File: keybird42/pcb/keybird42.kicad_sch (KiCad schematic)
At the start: 177 parts, among them SW111 SW_MX, SW112 SW_MX, SW113 SW_MX, SW114 SW_MX, SW115 SW_MX, SW116 SW_MX, SW117 SW_MX, SW121 SW_MX, SW122 SW_MX, SW123 SW_MX, SW124 SW_MX, SW125 SW_MX, SW126 SW_MX, SW127 SW_MX, SW131 SW_MX, SW132 SW_MX, SW133 SW_MX, SW134 SW_MX, SW135 SW_MX, SW136 SW_MX, SW137 SW_MX, SW211 SW_MX, SW212 SW_MX, SW213 SW_MX, SW214 SW_MX, SW215 SW_MX, SW216 SW_MX, SW217 SW_MX, SW221 SW_MX, SW222 SW_MX, SW223 SW_MX, SW225 SW_MX, SW226 SW_MX, SW227 SW_MX, SW231 SW_MX, SW232 SW_MX, SW233 SW_MX, SW234 SW_MX, SW235 SW_MX, SW236 SW_MX, SW237 SW_MX, SW311 SW_MX, SW312 SW_MX, SW314 SW_MX, SW315 SW_MX, SW316 SW_MX, SW317 SW_MX, SW321 SW_MX, SW322 SW_MX, SW323 SW_MX, SW324 SW_MX, SW325 SW_MX, SW327 SW_MX, SW331 SW_MX, SW332 SW_MX, SW333 SW_MX, SW334 SW_MX, SW335 SW_MX, SW336 SW_MX, SW337 SW_MX, SW411 SW_MX, SW412 SW_MX, SW413 SW_MX, SW414 SW_MX, SW415 SW_MX, SW416 SW_MX, SW417 SW_MX, SW421 SW_MX, SW422 SW_MX, SW423 SW_MX, SW424 SW_MX, SW425 SW_MX, SW426 SW_MX, SW427 SW_MX, SW431 SW_MX, SW432 SW_MX, SW433 SW_MX, SW434 SW_MX, SW435 SW_MX, SW436 SW_MX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

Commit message: rough positioning of row 4, two more holes
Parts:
- removed D422, D435: 1N4148W, Diode_SMD:D_SOD-123, symbol keybird42:1N4148W
- removed SW422, SW435: SW_MX, PCM_Switch_Keyboard_Hotswap_Kailh:SW_Hotswap_Kailh_MX, symbol keybird42:SW_MX
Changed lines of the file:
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@@
   (junction (at 113.03 177.8) (diameter 0) (color 0 0 0 0)
   )
-  (junction (at 57.15 152.4) (diameter 0) (color 0 0 0 0)
-  )
   (junction (at 74.93 157.48) (diameter 0) (color 0 0 0 0)
   )
@@
   (junction (at 57.15 76.2) (diameter 0) (color 0 0 0 0)
   )
-  (junction (at 46.99 144.78) (diameter 0) (color 0 0 0 0)
-  )
   (junction (at 43.18 177.8) (diameter 0) (color 0 0 0 0)
   )
@@
   (junction (at 113.03 63.5) (diameter 0) (color 0 0 0 0)
   )
-  (junction (at 99.06 165.1) (diameter 0) (color 0 0 0 0)
-  )
   (junction (at 74.93 55.88) (diameter 0) (color 0 0 0 0)
   )
@@
   (junction (at 60.96 55.88) (diameter 0) (color 0 0 0 0)
   )
-  (junction (at 88.9 157.48) (diameter 0) (color 0 0 0 0)
-  )
   (junction (at 71.12 127) (diameter 0) (color 0 0 0 0)
   )
@@
     (stroke (width 0) (type default))
   )
-  (wire (pts (xy 88.9 157.48) (xy 88.9 170.18))
+  (wire (pts (xy 88.9 144.78) (xy 88.9 170.18))
     (stroke (width 0) (type default))
   )
@@
     (stroke (width 0) (type default))
   )
-  (wire (pts (xy 85.09 165.1) (xy 99.06 165.1))
+  (wire (pts (xy 85.09 165.1) (xy 113.03 165.1))
     (stroke (width 0) (type default))
   )
@@
     (stroke (width 0) (type default))
   )
-  (wire (pts (xy 99.06 165.1) (xy 113.03 165.1))
-    (stroke (width 0) (type default))
-  )
-  (wire (pts (xy 46.99 144.78) (xy 46.99 157.48))
-    (stroke (width 0) (type default))
-  )
   (wire (pts (xy 57.15 177.8) (xy 71.12 177.8))
     (stroke (width 0) (type default))
@@
     (stroke (width 0) (type default))
   )
-  (wire (pts (xy 43.18 152.4) (xy 57.15 152.4))
-    (stroke (width 0) (type default))
-  )
   (wire (pts (xy 33.02 43.18) (xy 33.02 55.88))
     (stroke (width 0) (type default))
@@
     (stroke (width 0) (type default))
   )
-  (wire (pts (xy 46.99 132.08) (xy 46.99 144.78))
+  (wire (pts (xy 46.99 132.08) (xy 46.99 157.48))
     (stroke (width 0) (type default))
   )
@@
     (stroke (width 0) (type default))
   )
-  (wire (pts (xy 57.15 152.4) (xy 71.12 152.4))
+  (wire (pts (xy 43.18 152.4) (xy 71.12 152.4))
     (stroke (width 0) (type default))
   )
@@
     (stroke (width 0) (type default))
   )
-  (wire (pts (xy 88.9 144.78) (xy 88.9 157.48))
-    (stroke (width 0) (type default))
-  )
   (wire (pts (xy 85.09 114.3) (xy 99.06 114.3))
     (stroke (width 0) (type default))
@@
     )
   )
-  (symbol (lib_id "keybird42:SW_MX") (at 93.98 157.48 0) (unit 1)
-    (in_bom yes) (on_board yes) (dnp no)
-    (property "Reference" "SW435" (at 96.52 159.385 0) (do_not_autoplace)
-      (effects (font (size 1.27 1.27)) (justify right))
-    )
-    (property "Value" "SW_MX" (at 93.98 152.4 0)
-      (effects (font (size 1.27 1.27)) hide)
-    )
-    (property "Footprint" "PCM_Switch_Keyboard_Hotswap_Kailh:SW_Hotswap_Kailh_MX" (at 93.98 149.86 0)
-      (effects (font (size 1.27 1.27)) hide)
-    )
-    (property "Datasheet" "~" (at 93.98 152.4 0)
-      (effects (font (size 1.27 1.27)) hide)
-    )
-    (pin "2")
-    (pin "1")
-    (instances
-      (project "keybird42"
-        (path "/c6489b6f-cd36-4929-9d41-a438ed9c3e88"
-          (reference "SW435") (unit 1)
-        )
-      )
-    )
-  )
   (symbol (lib_id "keybird42:SW_MX") (at 93.98 17.78 0) (unit 1)
     (in_bom yes) (on_board yes) (dnp no)
@@
     )
   )
-  (symbol (lib_id "keybird42:SW_MX") (at 52.07 144.78 0) (unit 1)
-    (in_bom yes) (on_board yes) (dnp no)
-    (property "Reference" "SW422" (at 54.61 146.685 0) (do_not_autoplace)
-      (effects (font (size 1.27 1.27)) (justify right))
-    )
-    (property "Value" "SW_MX" (at 52.07 139.7 0)
-      (effects (font (size 1.27 1.27)) hide)
-    )
-    (property "Footprint" "PCM_Switch_Keyboard_Hotswap_Kailh:SW_Hotswap_Kailh_MX" (at 52.07 137.16 0)
-      (effects (font (size 1.27 1.27)) hide)
-    )
-    (property "Datasheet" "~" (at 52.07 139.7 0)
-      (effects (font (size 1.27 1.27)) hide)
-    )
-    (pin "2")
-    (pin "1")
-    (instances
-      (project "keybird42"
-        (path "/c6489b6f-cd36-4929-9d41-a438ed9c3e88"
-          (reference "SW422") (unit 1)
-        )
-      )
-    )
-  )
   (symbol (lib_id "keybird42:1N4148W") (at 57.15 59.69 0) (unit 1)
     (in_bom yes) (on_board yes) (dnp no) (fields_autoplaced)
@@
     )
   )
-  (symbol (lib_id "keybird42:1N4148W") (at 99.06 161.29 0) (unit 1)
-    (in_bom yes) (on_board yes) (dnp no) (fields_autoplaced)
-    (property "Reference" "D435" (at 96.52 162.56 0) (do_not_autoplace)
-      (effects (font (size 1.27 1.27)) (justify right))
-    )
-    (property "Value" "1N4148W" (at 99.06 168.91 0)
-      (effects (font (size 1.27 1.27)) hide)
-    )
-    (property "Footprint" "Diode_SMD:D_SOD-123" (at 99.06 171.45 0)
-      (effects (font (size 1.27 1.27)) hide)
-    )
-    (property "Datasheet" "https://www.vishay.com/docs/85748/1n4148w.pdf" (at 99.06 173.99 0)
-      (effects (font (size 1.27 1.27)) hide)
-    )
-    (property "Sim.Device" "D" (at 99.06 166.37 0)
-      (effects (font (size 1.27 1.27)) hide)
-    )
-    (property "Sim.Pins" "1=K 2=A" (at 102.87 161.29 90)
-      (effects (font (size 1.27 1.27)) hide)
-    )
-    (pin "1")
-    (pin "2")
-    (instances
-      (project "keybird42"
-        (path "/c6489b6f-cd36-4929-9d41-a438ed9c3e88"
-          (reference "D435") (unit 1)
-        )
-      )
-    )
-  )
   (symbol (lib_id "keybird42:1N4148W") (at 71.12 110.49 0) (unit 1)
     (in_bom yes) (on_board yes) (dnp no) (fields_autoplaced)
@@
         )
       )
-    )
-  )
-  (symbol (lib_id "keybird42:1N4148W") (at 57.15 148.59 0) (unit 1)
-    (in_bom yes) (on_board yes) (dnp no) (fields_autoplaced)
-    (property "Reference" "D422" (at 54.61 149.86 0) (do_not_autoplace)
-      (effects (font (size 1.27 1.27)) (justify right))
-    )
-    (property "Value" "1N4148W" (at 57.15 156.21 0)
-      (effects (font (size 1.27 1.27)) hide)
-    )
-    (property "Footprint" "Diode_SMD:D_SOD-123" (at 57.15 158.75 0)
-      (effects (font (size 1.27 1.27)) hide)
-    )
-    (property "Datasheet" "https://www.vishay.com/docs/85748/1n4148w.pdf" (at 57.15 161.29 0)
-      (effects (font (size 1.27 1.27)) hide)
-    )
-    (property "Sim.Device" "D" (at 57.15 153.67 0)
-      (effects (font (size 1.27 1.27)) hide)
-    )
-    (property "Sim.Pins" "1=K 2=A" (at 60.96 148.59 90)
-      (effects (font (size 1.27 1.27)) hide)
-    )
-    (pin "1")
-    (pin "2")
-    (instances
-      (project "keybird42"
-        (path "/c6489b6f-cd36-4929-9d41-a438ed9c3e88"
-          (reference "D422") (unit 1)
-        )
-      )

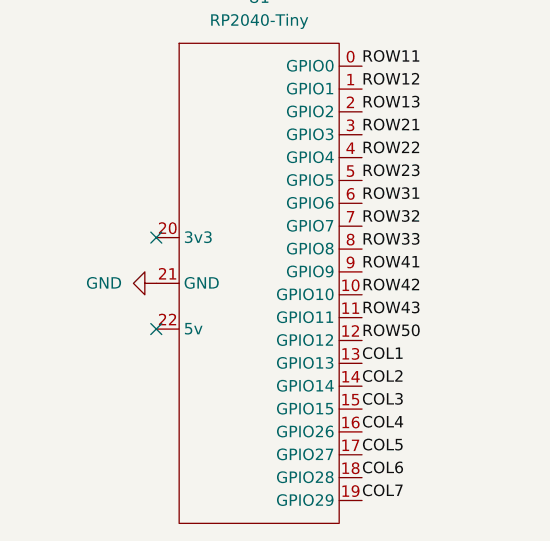
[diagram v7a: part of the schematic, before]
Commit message: more diode positioning
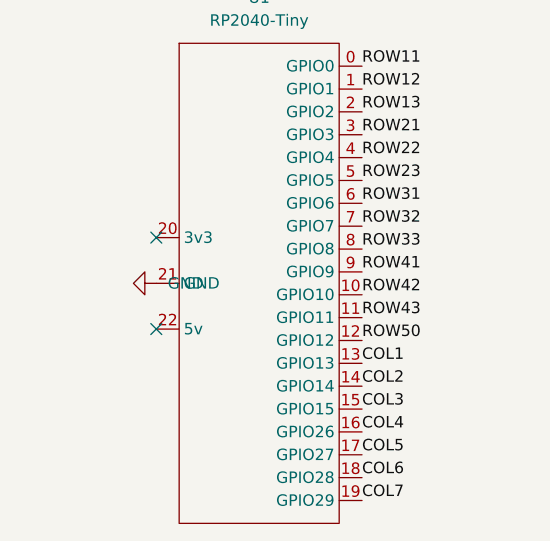
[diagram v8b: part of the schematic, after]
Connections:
- net COL1: now also SW111.2, SW121.2, SW131.2, SW211.2, SW221.2, SW231.2, SW311.2, SW321.2, SW331.2, SW411.2, SW421.2, SW431.2, SW501.2; no longer SW111.1, SW121.1, SW131.1, SW211.1, SW221.1, SW231.1, SW311.1, SW321.1, SW331.1, SW411.1, SW421.1, SW431.1, SW501.1
- net COL2: now also SW112.2, SW122.2, SW132.2, SW212.2, SW222.2, SW232.2, SW312.2, SW322.2, SW332.2, SW412.2, SW432.2, SW502.2; no longer SW112.1, SW122.1, SW132.1, SW212.1, SW222.1, SW232.1, SW312.1, SW322.1, SW332.1, SW412.1, SW432.1, SW502.1
- net COL3: now also SW113.2, SW123.2, SW133.2, SW213.2, SW223.2, SW233.2, SW323.2, SW333.2, SW413.2, SW423.2, SW433.2, SW503.2; no longer SW113.1, SW123.1, SW133.1, SW213.1, SW223.1, SW233.1, SW323.1, SW333.1, SW413.1, SW423.1, SW433.1, SW503.1
- net COL4: now also SW114.2, SW124.2, SW134.2, SW214.2, SW234.2, SW314.2, SW324.2, SW334.2, SW414.2, SW424.2, SW434.2, SW504.2; no longer SW114.1, SW124.1, SW134.1, SW214.1, SW234.1, SW314.1, SW324.1, SW334.1, SW414.1, SW424.1, SW434.1, SW504.1
- net COL5: now also SW115.2, SW125.2, SW135.2, SW215.2, SW225.2, SW235.2, SW315.2, SW325.2, SW335.2, SW415.2, SW425.2, SW505.2; no longer SW115.1, SW125.1, SW135.1, SW215.1, SW225.1, SW235.1, SW315.1, SW325.1, SW335.1, SW415.1, SW425.1, SW505.1
- net COL6: now also SW116.2, SW126.2, SW136.2, SW216.2, SW226.2, SW236.2, SW316.2, SW336.2, SW416.2, SW426.2, SW436.2, SW506.2; no longer SW116.1, SW126.1, SW136.1, SW216.1, SW226.1, SW236.1, SW316.1, SW336.1, SW416.1, SW426.1, SW436.1, SW506.1
- net COL7: now also SW117.2, SW127.2, SW137.2, SW217.2, SW227.2, SW237.2, SW317.2, SW327.2, SW337.2, SW417.2, SW427.2, SW437.2, SW507.2; no longer SW117.1, SW127.1, SW137.1, SW217.1, SW227.1, SW237.1, SW317.1, SW327.1, SW337.1, SW417.1, SW427.1, SW437.1, SW507.1
- net at D327.2 (A): now also SW327.1; no longer SW327.2
- net at D423.2 (A): now also SW423.1; no longer SW423.2
- net at D436.2 (A): now also SW436.1; no longer SW436.2
- net at D214.2 (A): now also SW214.1; no longer SW214.2
- net at D505.2 (A): now also SW505.1; no longer SW505.2
- net at D416.2 (A): now also SW416.1; no longer SW416.2
- net at D115.2 (A): now also SW115.1; no longer SW115.2
- net at D417.2 (A): now also SW417.1; no longer SW417.2
- net at D215.2 (A): now also SW215.1; no longer SW215.2
- net at D431.2 (A): now also SW431.1; no longer SW431.2
- net at D227.2 (A): now also SW227.1; no longer SW227.2
- net at D427.2 (A): now also SW427.1; no longer SW427.2
- net at D211.2 (A): now also SW211.1; no longer SW211.2
- net at D412.2 (A): now also SW412.1; no longer SW412.2
- net at D503.2 (A): now also SW503.1; no longer SW503.2
- net at D135.2 (A): now also SW135.1; no longer SW135.2
- net at D223.2 (A): now also SW223.1; no longer SW223.2
- net at D323.2 (A): now also SW323.1; no longer SW323.2
- net at D321.2 (A): now also SW321.1; no longer SW321.2
- net at D213.2 (A): now also SW213.1; no longer SW213.2
- net at D235.2 (A): now also SW235.1; no longer SW235.2
- net at D425.2 (A): now also SW425.1; no longer SW425.2
- net at D315.2 (A): now also SW315.1; no longer SW315.2
- net at D316.2 (A): now also SW316.1; no longer SW316.2
- net at D314.2 (A): now also SW314.1; no longer SW314.2
- net at D133.2 (A): now also SW133.1; no longer SW133.2
- net at D432.2 (A): now also SW432.1; no longer SW432.2
- net at D311.2 (A): now also SW311.1; no longer SW311.2
- net at D335.2 (A): now also SW335.1; no longer SW335.2
- net at D332.2 (A): now also SW332.1; no longer SW332.2
- net at D212.2 (A): now also SW212.1; no longer SW212.2
- net at D117.2 (A): now also SW117.1; no longer SW117.2
- net at D413.2 (A): now also SW413.1; no longer SW413.2
- net at D113.2 (A): now also SW113.1; no longer SW113.2
- net at D114.2 (A): now also SW114.1; no longer SW114.2
- net at D226.2 (A): now also SW226.1; no longer SW226.2
- net at D222.2 (A): now also SW222.1; no longer SW222.2
- net at D221.2 (A): now also SW221.1; no longer SW221.2
- net at D122.2 (A): now also SW122.1; no longer SW122.2
- net at D434.2 (A): now also SW434.1; no longer SW434.2
- net at D415.2 (A): now also SW415.1; no longer SW415.2
- net at D124.2 (A): now also SW124.1; no longer SW124.2
- net at D234.2 (A): now also SW234.1; no longer SW234.2
- net at D437.2 (A): now also SW437.1; no longer SW437.2
- net at D121.2 (A): now also SW121.1; no longer SW121.2
- net at D137.2 (A): now also SW137.1; no longer SW137.2
- net at D414.2 (A): now also SW414.1; no longer SW414.2
- net at D506.2 (A): now also SW506.1; no longer SW506.2
- net at D217.2 (A): now also SW217.1; no longer SW217.2
- net at D331.2 (A): now also SW331.1; no longer SW331.2
- net at D336.2 (A): now also SW336.1; no longer SW336.2
- net at D233.2 (A): now also SW233.1; no longer SW233.2
- net at D501.2 (A): now also SW501.1; no longer SW501.2
- net at D236.2 (A): now also SW236.1; no longer SW236.2
- net at D433.2 (A): now also SW433.1; no longer SW433.2
- net at D123.2 (A): now also SW123.1; no longer SW123.2
- net at D317.2 (A): now also SW317.1; no longer SW317.2
- net at D334.2 (A): now also SW334.1; no longer SW334.2
- net at D337.2 (A): now also SW337.1; no longer SW337.2
- net at D333.2 (A): now also SW333.1; no longer SW333.2
- net at D131.2 (A): now also SW131.1; no longer SW131.2
- net at D411.2 (A): now also SW411.1; no longer SW411.2
- net at D232.2 (A): now also SW232.1; no longer SW232.2
- net at D502.2 (A): now also SW502.1; no longer SW502.2
- net at D507.2 (A): now also SW507.1; no longer SW507.2
- net at D126.2 (A): now also SW126.1; no longer SW126.2
- net at D127.2 (A): now also SW127.1; no longer SW127.2
- net at D136.2 (A): now also SW136.1; no longer SW136.2
- net at D132.2 (A): now also SW132.1; no longer SW132.2
- net at D134.2 (A): now also SW134.1; no longer SW134.2
- net at D225.2 (A): now also SW225.1; no longer SW225.2
- net at D237.2 (A): now also SW237.1; no longer SW237.2
- net at D324.2 (A): now also SW324.1; no longer SW324.2
- net at D216.2 (A): now also SW216.1; no longer SW216.2
- net at D421.2 (A): now also SW421.1; no longer SW421.2
- net at D322.2 (A): now also SW322.1; no longer SW322.2
- net at D112.2 (A): now also SW112.1; no longer SW112.2
- net at D424.2 (A): now also SW424.1; no longer SW424.2
- net at D312.2 (A): now also SW312.1; no longer SW312.2
- net at D111.2 (A): now also SW111.1; no longer SW111.2
- net at D116.2 (A): now also SW116.1; no longer SW116.2
- net at D325.2 (A): now also SW325.1; no longer SW325.2
- net at D504.2 (A): now also SW504.1; no longer SW504.2
- net at D231.2 (A): now also SW231.1; no longer SW231.2
- net at D125.2 (A): now also SW125.1; no longer SW125.2
- net at D426.2 (A): now also SW426.1; no longer SW426.2
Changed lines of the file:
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@@
       (effects (font (size 1.27 1.27)) hide)
     )
-    (property "Value" "GND" (at 29.21 241.3 90)
-      (effects (font (size 1.27 1.27)) (justify right))
+    (property "Value" "GND" (at 34.29 241.3 90)
+      (effects (font (size 1.27 1.27)) (justify left))
     )
     (property "Footprint" "" (at 33.02 241.3 0)
